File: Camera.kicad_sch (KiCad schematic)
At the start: 0 parts

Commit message: PMIC DCDC
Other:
- title: Leaf RV1126 Power -> Leaf RV1126 PMIC RK809
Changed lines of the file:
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@@
   (paper "A4")
   (title_block
-    (title "Leaf RV1126 Power")
+    (title "Leaf RV1126 PMIC RK809")
     (date "2023-02-23")
     (rev "1")

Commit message: updated: PMIC codec
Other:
- title: Leaf RV1126 PMIC RK809 -> Leaf RV1126 PMIC RK809 Codec
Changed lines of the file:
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@@
   (paper "A4")
   (title_block
-    (title "Leaf RV1126 PMIC RK809")
-    (date "2023-02-23")
+    (title "Leaf RV1126 PMIC RK809 Codec")
+    (date "2023-02-25")
     (rev "1")
     (company "Qingdao IotPi Information Technology")

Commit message: updated: titles
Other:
- title: Leaf RV1126 PMIC RK809 Codec -> Leaf RV1126 RK809 Camera
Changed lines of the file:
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@@
   (paper "A4")
   (title_block
-    (title "Leaf RV1126 PMIC RK809 Codec")
+    (title "Leaf RV1126 RK809 Camera")
     (date "2023-02-25")
     (rev "1")

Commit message: added Camera MIPI CSI
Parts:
- added C57 (x3): 100nF X5R 16V, Capacitor_SMD:C_0402_1005Metric, symbol Device:C
- added C57 (x2): 10uF X5R 6.3V, Capacitor_SMD:C_0603_1608Metric, symbol Device:C
- added C57 (x3): 100nF X5R 6.3V, Capacitor_SMD:C_0201_0603Metric, symbol Device:C
- added J3: MIPI-CSI, symbol Connector:Conn_01x24_Pin
- added R40 (x2): 0R 5%, Resistor_SMD:R_0402_1005Metric, symbol Device:R
- added R40 (x2): 2.2K 5%, Resistor_SMD:R_0402_1005Metric, symbol Device:R
- added U1: rv1126/rv1109, symbol CPU_Rockchip:rv1126_rv1109
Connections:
- new net GND: C57.2, C57.2, C57.2, C57.2, C57.2, C57.2, C57.2, C57.2, J3.1 (Pin_1), J3.17 (Pin_17), J3.2 (Pin_2), J3.20 (Pin_20), J3.7 (Pin_7), J3.8 (Pin_8)
- new net MIPI_CSI_AVDD_0V8: C57.1, R40.2, U1.T15 (MIPI_CSI_RX0_AVDD_0V8)
- new net MIPI_CSI_AVDD_1V8: C57.1, R40.2, U1.T16 (MIPI_CSI_RX0_AVDD_1V8)
- new net MIPI_CSI_I2C_SCL: J3.6 (Pin_6), R40.1, U1.Y21 (I2C1_SCL/UART4_CTSN_M2/GPIO1_D3_u)
- new net MIPI_CSI_I2C_SDA: J3.5 (Pin_5), R40.1, U1.W19 (I2C1_SDA/UART4_RTSN_M2/GPIO1_D2_u)
- new net MIPI_CSI_MCLK0: J3.21 (Pin_21), U1.V21 (MIPI_CSI_CLK0/UART5_CTSN_M2/GPIO2_A3_d)
- new net MIPI_CSI_PWR0: J3.3 (Pin_3), U1.W20 (UART4_RX_M2/GPIO1_D4_d)
- new net MIPI_CSI_RST0: J3.4 (Pin_4), U1.V19 (SPI0_MOSI_M1/I2S1_SCLK_M1/I2C3_SCL_M2/GPIO1_D6_d)
- new net MIPI_RX0_CLKN: J3.18 (Pin_18), U1.V15 (MIPI_CSI_RX0_CLKN/LVDS0_CLKN)
- new net MIPI_RX0_CLKP: J3.19 (Pin_19), U1.U15 (MIPI_CSI_RX0_CLKP/LVDS0_CLKP)
- new net MIPI_RX0_D0N: J3.9 (Pin_9), U1.U16 (MIPI_CSI_RX0_D0N/LVDS0_RX0N)
- new net MIPI_RX0_D0P: J3.10 (Pin_10), U1.V16 (MIPI_CSI_RX0_D0P/LVDS0_RX0P)
- new net MIPI_RX0_D1N: J3.11 (Pin_11), U1.W16 (MIPI_CSI_RX0_D1N/LVDS0_RX1N)
- new net MIPI_RX0_D1P: J3.12 (Pin_12), U1.Y16 (MIPI_CSI_RX0_D1P/LVDS0_RX1P)
- new net MIPI_RX0_D2N: J3.13 (Pin_13), U1.Y15 (MIPI_CSI_RX0_D2N/LVDS0_RX2N)
- new net MIPI_RX0_D2P: J3.14 (Pin_14), U1.W15 (MIPI_CSI_RX0_D2P/LVDS0_RX2P)
- new net MIPI_RX0_D3N: J3.15 (Pin_15), U1.AA16 (MIPI_CSI_RX0_D3N/LVDS0_RX3N)
- new net MIPI_RX0_D3P: J3.16 (Pin_16), U1.AA15 (MIPI_CSI_RX0_D3P/LVDS0_RX3P)
- new net VCC1V8_DOVDD: C57.1, J3.22 (Pin_22), R40.2, R40.2
- new net VCCAVDD_RGB: C57.1, C57.1, J3.24 (Pin_24)
- new net VCCDVDD_RGB: C57.1, C57.1, J3.23 (Pin_23)
- new net VCC_0V8: R40.1
- new net VCC_1V8: C57.1, R40.1, U1.P15 (VCCIO4_VDD)
- no-connect marks 0 -> 17

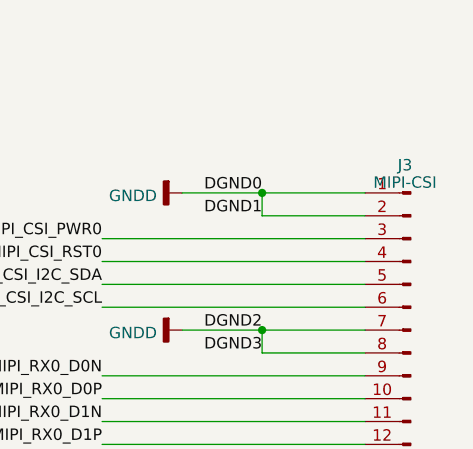
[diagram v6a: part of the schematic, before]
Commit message: updated footprints
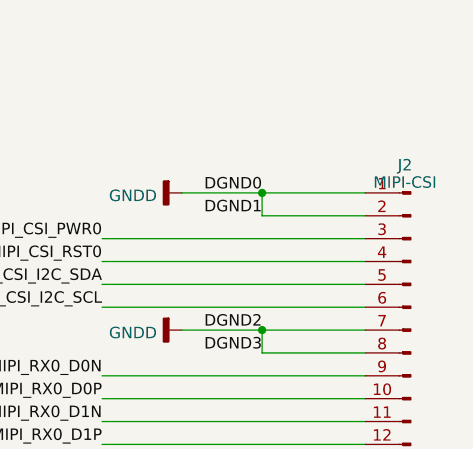
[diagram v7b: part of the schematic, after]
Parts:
- U1: footprint (none) -> Rockchip_SoC:Rockchip_RV1126_FCCSP409LD_14.0x14.0mm
- renumbered J3 to J2
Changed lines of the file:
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@@
   (symbol (lib_id "power:GNDA") (at 123.19 184.15 0) (unit 1)
     (in_bom yes) (on_board yes) (dnp no) (fields_autoplaced)
-    (property "Reference" "#PWR0102" (at 123.19 190.5 0)
+    (property "Reference" "#PWR022" (at 123.19 190.5 0)
       (effects (font (size 1.27 1.27)) hide)
     )
@@
       (project "leaf"
         (path "/e3b58043-16a3-43c8-9fad-9c9784eebfa4/bca9f05a-f031-46a4-95a9-25be55b42bf6"
-          (reference "#PWR0102") (unit 1)
+          (reference "#PWR022") (unit 1)
         )
       )
@@
         )
         (path "/e3b58043-16a3-43c8-9fad-9c9784eebfa4/bca9f05a-f031-46a4-95a9-25be55b42bf6"
-          (reference "C125") (unit 1)
+          (reference "C20") (unit 1)
         )
       )
@@
         )
         (path "/e3b58043-16a3-43c8-9fad-9c9784eebfa4/bca9f05a-f031-46a4-95a9-25be55b42bf6"
-          (reference "R58") (unit 1)
+          (reference "R23") (unit 1)
         )
       )
@@
   (symbol (lib_id "Connector:Conn_01x24_Pin") (at 275.59 68.58 0) (mirror y) (unit 1)
     (in_bom yes) (on_board yes) (dnp no)
-    (property "Reference" "J3" (at 274.955 37.5539 0)
+    (property "Reference" "J2" (at 274.955 37.5539 0)
       (effects (font (size 1.27 1.27)))
     )
@@
       (project "leaf"
         (path "/e3b58043-16a3-43c8-9fad-9c9784eebfa4/bca9f05a-f031-46a4-95a9-25be55b42bf6"
-          (reference "J3") (unit 1)
+          (reference "J2") (unit 1)
         )
       )
@@
   (symbol (lib_id "power:GND") (at 148.59 184.15 0) (unit 1)
     (in_bom yes) (on_board yes) (dnp no) (fields_autoplaced)
-    (property "Reference" "#PWR0108" (at 148.59 190.5 0)
+    (property "Reference" "#PWR024" (at 148.59 190.5 0)
       (effects (font (size 1.27 1.27)) hide)
     )
@@
       (project "leaf"
         (path "/e3b58043-16a3-43c8-9fad-9c9784eebfa4/bca9f05a-f031-46a4-95a9-25be55b42bf6"
-          (reference "#PWR0108") (unit 1)
+          (reference "#PWR024") (unit 1)
         )
       )
@@
         )
         (path "/e3b58043-16a3-43c8-9fad-9c9784eebfa4/bca9f05a-f031-46a4-95a9-25be55b42bf6"
-          (reference "R60") (unit 1)
+          (reference "R20") (unit 1)
         )
       )
@@
         )
         (path "/e3b58043-16a3-43c8-9fad-9c9784eebfa4/bca9f05a-f031-46a4-95a9-25be55b42bf6"
-          (reference "C122") (unit 1)
+          (reference "C18") (unit 1)
         )
       )
@@
         )
         (path "/e3b58043-16a3-43c8-9fad-9c9784eebfa4/bca9f05a-f031-46a4-95a9-25be55b42bf6"
-          (reference "C124") (unit 1)
+          (reference "C14") (unit 1)
         )
       )
@@
         )
         (path "/e3b58043-16a3-43c8-9fad-9c9784eebfa4/bca9f05a-f031-46a4-95a9-25be55b42bf6"
-          (reference "C121") (unit 1)
+          (reference "C17") (unit 1)
         )
       )
@@
         )
         (path "/e3b58043-16a3-43c8-9fad-9c9784eebfa4/bca9f05a-f031-46a4-95a9-25be55b42bf6"
-          (reference "C119") (unit 1)
+          (reference "C13") (unit 1)
         )
       )
@@
         )
         (path "/e3b58043-16a3-43c8-9fad-9c9784eebfa4/bca9f05a-f031-46a4-95a9-25be55b42bf6"
-          (reference "C118") (unit 1)
+          (reference "C15") (unit 1)
         )
       )
@@
         )
         (path "/e3b58043-16a3-43c8-9fad-9c9784eebfa4/bca9f05a-f031-46a4-95a9-25be55b42bf6"
-          (reference "#PWR0105") (unit 1)
+          (reference "#PWR030") (unit 1)
         )
       )
@@
         )
         (path "/e3b58043-16a3-43c8-9fad-9c9784eebfa4/bca9f05a-f031-46a4-95a9-25be55b42bf6"
-          (reference "#PWR0104") (unit 1)
+          (reference "#PWR025") (unit 1)
         )
       )
@@
         )
         (path "/e3b58043-16a3-43c8-9fad-9c9784eebfa4/bca9f05a-f031-46a4-95a9-25be55b42bf6"
-          (reference "#PWR0106") (unit 1)
+          (reference "#PWR031") (unit 1)
         )
       )
@@
   (symbol (lib_id "power:GNDA") (at 109.22 185.42 0) (mirror y) (unit 1)
     (in_bom yes) (on_board yes) (dnp no) (fields_autoplaced)
-    (property "Reference" "#PWR0100" (at 109.22 191.77 0)
+    (property "Reference" "#PWR021" (at 109.22 191.77 0)
       (effects (font (size 1.27 1.27)) hide)
     )
@@
       (project "leaf"
         (path "/e3b58043-16a3-43c8-9fad-9c9784eebfa4/bca9f05a-f031-46a4-95a9-25be55b42bf6"
-          (reference "#PWR0100") (unit 1)
+          (reference "#PWR021") (unit 1)
         )
       )
@@
   (symbol (lib_id "power:GNDA") (at 64.77 184.15 0) (mirror y) (unit 1)
     (in_bom yes) (on_board yes) (dnp no) (fields_autoplaced)
-    (property "Reference" "#PWR0101" (at 64.77 190.5 0)
+    (property "Reference" "#PWR019" (at 64.77 190.5 0)
       (effects (font (size 1.27 1.27)) hide)
     )
@@
       (project "leaf"
         (path "/e3b58043-16a3-43c8-9fad-9c9784eebfa4/bca9f05a-f031-46a4-95a9-25be55b42bf6"
-          (reference "#PWR0101") (unit 1)
+          (reference "#PWR019") (unit 1)
         )
       )
@@
   (symbol (lib_id "power:GNDD") (at 250.19 40.64 270) (unit 1)
     (in_bom yes) (on_board yes) (dnp no) (fields_autoplaced)
-    (property "Reference" "#PWR096" (at 243.84 40.64 0)
+    (property "Reference" "#PWR026" (at 243.84 40.64 0)
       (effects (font (size 1.27 1.27)) hide)
     )
@@
       (project "leaf"
         (path "/e3b58043-16a3-43c8-9fad-9c9784eebfa4/bca9f05a-f031-46a4-95a9-25be55b42bf6"
-          (reference "#PWR096") (unit 1)
+          (reference "#PWR026") (unit 1)
         )
       )
@@
   (symbol (lib_id "power:GNDD") (at 250.19 88.9 270) (unit 1)
     (in_bom yes) (on_board yes) (dnp no) (fields_autoplaced)
-    (property "Reference" "#PWR099" (at 243.84 88.9 0)
+    (property "Reference" "#PWR029" (at 243.84 88.9 0)
       (effects (font (size 1.27 1.27)) hide)
     )
@@
       (project "leaf"
         (path "/e3b58043-16a3-43c8-9fad-9c9784eebfa4/bca9f05a-f031-46a4-95a9-25be55b42bf6"
-          (reference "#PWR099") (unit 1)
+          (reference "#PWR029") (unit 1)
         )
       )
@@
         )
         (path "/e3b58043-16a3-43c8-9fad-9c9784eebfa4/bca9f05a-f031-46a4-95a9-25be55b42bf6"
-          (reference "R61") (unit 1)
+          (reference "R21") (unit 1)
         )
       )
@@
         )
         (path "/e3b58043-16a3-43c8-9fad-9c9784eebfa4/bca9f05a-f031-46a4-95a9-25be55b42bf6"
-          (reference "C120") (unit 1)
+          (reference "C16") (unit 1)
         )
       )
@@
   (symbol (lib_id "power:GND") (at 96.52 83.82 0) (unit 1)
     (in_bom yes) (on_board yes) (dnp no) (fields_autoplaced)
-    (property "Reference" "#PWR0107" (at 96.52 90.17 0)
+    (property "Reference" "#PWR020" (at 96.52 90.17 0)
       (effects (font (size 1.27 1.27)) hide)
     )
@@
       (project "leaf"
         (path "/e3b58043-16a3-43c8-9fad-9c9784eebfa4/bca9f05a-f031-46a4-95a9-25be55b42bf6"
-          (reference "#PWR0107") (unit 1)
+          (reference "#PWR020") (unit 1)
         )
       )
@@
   (symbol (lib_id "power:GNDD") (at 250.19 81.28 270) (unit 1)
     (in_bom yes) (on_board yes) (dnp no) (fields_autoplaced)
-    (property "Reference" "#PWR098" (at 243.84 81.28 0)
+    (property "Reference" "#PWR028" (at 243.84 81.28 0)
       (effects (font (size 1.27 1.27)) hide)
     )
@@
       (project "leaf"
         (path "/e3b58043-16a3-43c8-9fad-9c9784eebfa4/bca9f05a-f031-46a4-95a9-25be55b42bf6"
-          (reference "#PWR098") (unit 1)
+          (reference "#PWR028") (unit 1)
         )
       )
@@
   (symbol (lib_id "power:GNDD") (at 250.19 55.88 270) (unit 1)
     (in_bom yes) (on_board yes) (dnp no) (fields_autoplaced)
-    (property "Reference" "#PWR097" (at 243.84 55.88 0)
+    (property "Reference" "#PWR027" (at 243.84 55.88 0)
       (effects (font (size 1.27 1.27)) hide)
     )
@@
       (project "leaf"
         (path "/e3b58043-16a3-43c8-9fad-9c9784eebfa4/bca9f05a-f031-46a4-95a9-25be55b42bf6"
-          (reference "#PWR097") (unit 1)
+          (reference "#PWR027") (unit 1)
         )
       )
@@
   (symbol (lib_id "power:GNDD") (at 135.89 184.15 0) (unit 1)
     (in_bom yes) (on_board yes) (dnp no) (fields_autoplaced)
-    (property "Reference" "#PWR0103" (at 135.89 190.5 0)
+    (property "Reference" "#PWR023" (at 135.89 190.5 0)
       (effects (font (size 1.27 1.27)) hide)
     )
@@
       (project "leaf"
         (path "/e3b58043-16a3-43c8-9fad-9c9784eebfa4/bca9f05a-f031-46a4-95a9-25be55b42bf6"
-          (reference "#PWR0103") (unit 1)
+          (reference "#PWR023") (unit 1)
         )
       )
@@
       (effects (font (size 1.27 1.27)))
     )
-    (property "Footprint" "" (at 87.63 83.82 0)
+    (property "Footprint" "Rockchip_SoC:Rockchip_RV1126_FCCSP409LD_14.0x14.0mm" (at 87.63 83.82 0)
       (effects (font (size 1.27 1.27)) hide)
     )
@@
         )
         (path "/e3b58043-16a3-43c8-9fad-9c9784eebfa4/bca9f05a-f031-46a4-95a9-25be55b42bf6"
-          (reference "R59") (unit 1)
+          (reference "R22") (unit 1)
         )
       )
@@
       (effects (font (size 1.27 1.27)))
     )
-    (property "Footprint" "" (at 193.04 83.82 0)
+    (property "Footprint" "Rockchip_SoC:Rockchip_RV1126_FCCSP409LD_14.0x14.0mm" (at 193.04 83.82 0)
       (effects (font (size 1.27 1.27)) hide)
     )
@@
         )
         (path "/e3b58043-16a3-43c8-9fad-9c9784eebfa4/bca9f05a-f031-46a4-95a9-25be55b42bf6"
-          (reference "C123") (unit 1)
-        )
-      )
+          (reference "C19") (unit 1)
+        )
+      )

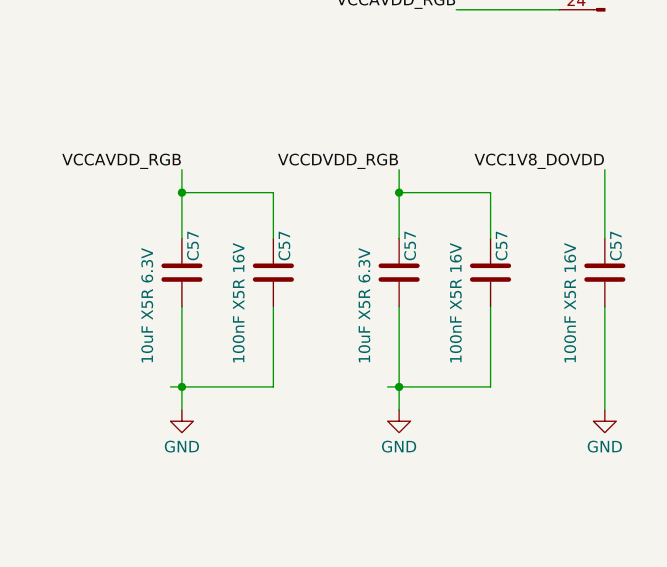
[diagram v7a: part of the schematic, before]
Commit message: updated Capacitors
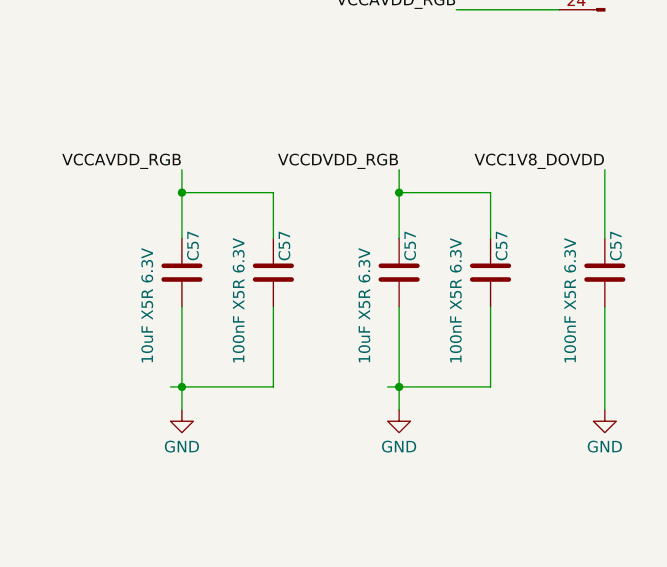
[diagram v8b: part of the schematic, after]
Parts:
- C57: value 100nF X5R 16V -> 100nF X5R 6.3V; footprint Capacitor_SMD:C_0402_1005Metric -> Capacitor_SMD:C_0201_0603Metric; LCSC (none) -> C76934; Model (none) -> GRM033R61A104KE15D; Vendor (none) -> muRata(村田)
- C57: LCSC (none) -> C76934; Model (none) -> GRM033R61A104KE15D; Vendor (none) -> muRata(村田)
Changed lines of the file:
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@@
       (effects (font (size 1.27 1.27)) (justify left))
     )
-    (property "Value" "100nF X5R 16V" (at 271.78 138.43 90)
+    (property "Value" "100nF X5R 6.3V" (at 271.78 138.43 90)
       (effects (font (size 1.27 1.27)) (justify left))
     )
-    (property "Footprint" "Capacitor_SMD:C_0402_1005Metric" (at 276.5552 132.08 0)
+    (property "Footprint" "Capacitor_SMD:C_0201_0603Metric" (at 276.5552 132.08 0)
       (effects (font (size 1.27 1.27)) hide)
     )
     (property "Datasheet" "~" (at 275.59 128.27 0)
+      (effects (font (size 1.27 1.27)) hide)
+    )
+    (property "Description" "容值: 100nF 精度: ±10% 额定电压: 10V 材质(温度系数): X5R 材质:X5R" (at 275.59 128.27 0)
+      (effects (font (size 1.27 1.27)) hide)
+    )
+    (property "LCSC" "C76934" (at 275.59 128.27 0)
+      (effects (font (size 1.27 1.27)) hide)
+    )
+    (property "Model" "GRM033R61A104KE15D" (at 275.59 128.27 0)
+      (effects (font (size 1.27 1.27)) hide)
+    )
+    (property "Vendor" "muRata(村田)" (at 275.59 128.27 0)
       (effects (font (size 1.27 1.27)) hide)
     )
@@
       (effects (font (size 1.27 1.27)) hide)
     )
+    (property "Description" "容值: 100nF 精度: ±10% 额定电压: 10V 材质(温度系数): X5R 材质:X5R" (at 96.52 77.47 0)
+      (effects (font (size 1.27 1.27)) hide)
+    )
+    (property "LCSC" "C76934" (at 96.52 77.47 0)
+      (effects (font (size 1.27 1.27)) hide)
+    )
+    (property "Model" "GRM033R61A104KE15D" (at 96.52 77.47 0)
+      (effects (font (size 1.27 1.27)) hide)
+    )
+    (property "Vendor" "muRata(村田)" (at 96.52 77.47 0)
+      (effects (font (size 1.27 1.27)) hide)
+    )
     (pin "1")
     (pin "2")
@@
       (effects (font (size 1.27 1.27)) (justify left))
     )
-    (property "Value" "100nF X5R 16V" (at 234.95 138.43 90)
+    (property "Value" "100nF X5R 6.3V" (at 234.95 138.43 90)
       (effects (font (size 1.27 1.27)) (justify left))
     )
-    (property "Footprint" "Capacitor_SMD:C_0402_1005Metric" (at 239.7252 132.08 0)
+    (property "Footprint" "Capacitor_SMD:C_0201_0603Metric" (at 239.7252 132.08 0)
       (effects (font (size 1.27 1.27)) hide)
     )
     (property "Datasheet" "~" (at 238.76 128.27 0)
+      (effects (font (size 1.27 1.27)) hide)
+    )
+    (property "Description" "容值: 100nF 精度: ±10% 额定电压: 10V 材质(温度系数): X5R 材质:X5R" (at 238.76 128.27 0)
+      (effects (font (size 1.27 1.27)) hide)
+    )
+    (property "LCSC" "C76934" (at 238.76 128.27 0)
+      (effects (font (size 1.27 1.27)) hide)
+    )
+    (property "Model" "GRM033R61A104KE15D" (at 238.76 128.27 0)
+      (effects (font (size 1.27 1.27)) hide)
+    )
+    (property "Vendor" "muRata(村田)" (at 238.76 128.27 0)
       (effects (font (size 1.27 1.27)) hide)
     )
@@
       (effects (font (size 1.27 1.27)) hide)
     )
+    (property "Description" "容值: 100nF 精度: ±10% 额定电压: 10V 材质(温度系数): X5R 材质:X5R" (at 64.77 177.8 0)
+      (effects (font (size 1.27 1.27)) hide)
+    )
+    (property "LCSC" "C76934" (at 64.77 177.8 0)
+      (effects (font (size 1.27 1.27)) hide)
+    )
+    (property "Model" "GRM033R61A104KE15D" (at 64.77 177.8 0)
+      (effects (font (size 1.27 1.27)) hide)
+    )
+    (property "Vendor" "muRata(村田)" (at 64.77 177.8 0)
+      (effects (font (size 1.27 1.27)) hide)
+    )
     (pin "1")
     (pin "2")
@@
     )
     (property "Datasheet" "~" (at 109.22 179.07 0)
+      (effects (font (size 1.27 1.27)) hide)
+    )
+    (property "Description" "容值: 100nF 精度: ±10% 额定电压: 10V 材质(温度系数): X5R 材质:X5R" (at 109.22 179.07 0)
+      (effects (font (size 1.27 1.27)) hide)
+    )
+    (property "LCSC" "C76934" (at 109.22 179.07 0)
+      (effects (font (size 1.27 1.27)) hide)
+    )
+    (property "Model" "GRM033R61A104KE15D" (at 109.22 179.07 0)
+      (effects (font (size 1.27 1.27)) hide)
+    )
+    (property "Vendor" "muRata(村田)" (at 109.22 179.07 0)
       (effects (font (size 1.27 1.27)) hide)
     )
@@
       (effects (font (size 1.27 1.27)) (justify left))
     )
-    (property "Value" "100nF X5R 16V" (at 259.08 138.43 90)
+    (property "Value" "100nF X5R 6.3V" (at 259.08 138.43 90)
       (effects (font (size 1.27 1.27)) (justify left))
     )
-    (property "Footprint" "Capacitor_SMD:C_0402_1005Metric" (at 263.8552 132.08 0)
+    (property "Footprint" "Capacitor_SMD:C_0201_0603Metric" (at 263.8552 132.08 0)
       (effects (font (size 1.27 1.27)) hide)
     )
@@
       (effects (font (size 1.27 1.27)) hide)
     )
+    (property "Description" "容值: 100nF 精度: ±10% 额定电压: 10V 材质(温度系数): X5R 材质:X5R" (at 262.89 128.27 0)
+      (effects (font (size 1.27 1.27)) hide)
+    )
+    (property "LCSC" "C76934" (at 262.89 128.27 0)
+      (effects (font (size 1.27 1.27)) hide)
+    )
+    (property "Model" "GRM033R61A104KE15D" (at 262.89 128.27 0)
+      (effects (font (size 1.27 1.27)) hide)
+    )
+    (property "Vendor" "muRata(村田)" (at 262.89 128.27 0)
+      (effects (font (size 1.27 1.27)) hide)
+    )
